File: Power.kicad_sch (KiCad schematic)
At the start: 12 parts, among them J201 Barrel_Jack, U201 AMS1117-3.3, U202 AMS1117-5.0, U203 AMS1117-3.3

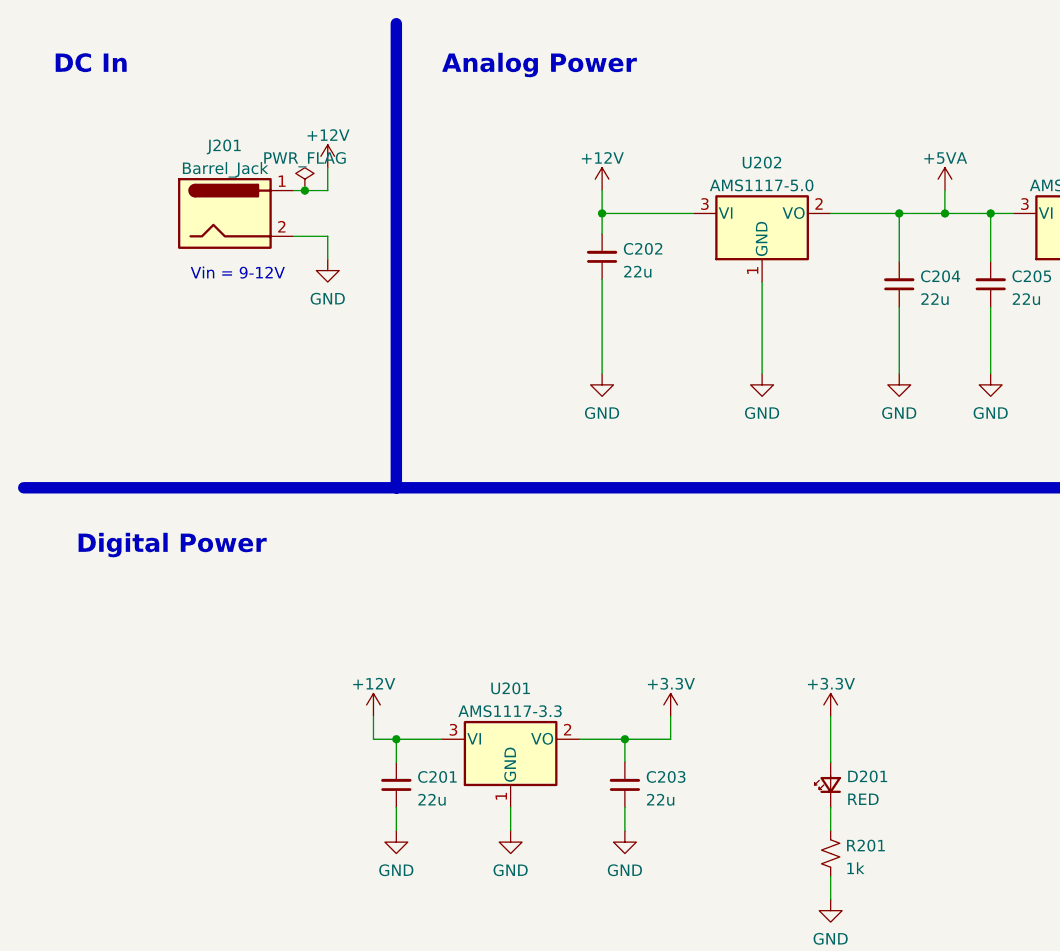
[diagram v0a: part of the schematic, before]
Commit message: Switch ADC
Switched from the ADS1115 to ADS7924 to get faster sampling time.
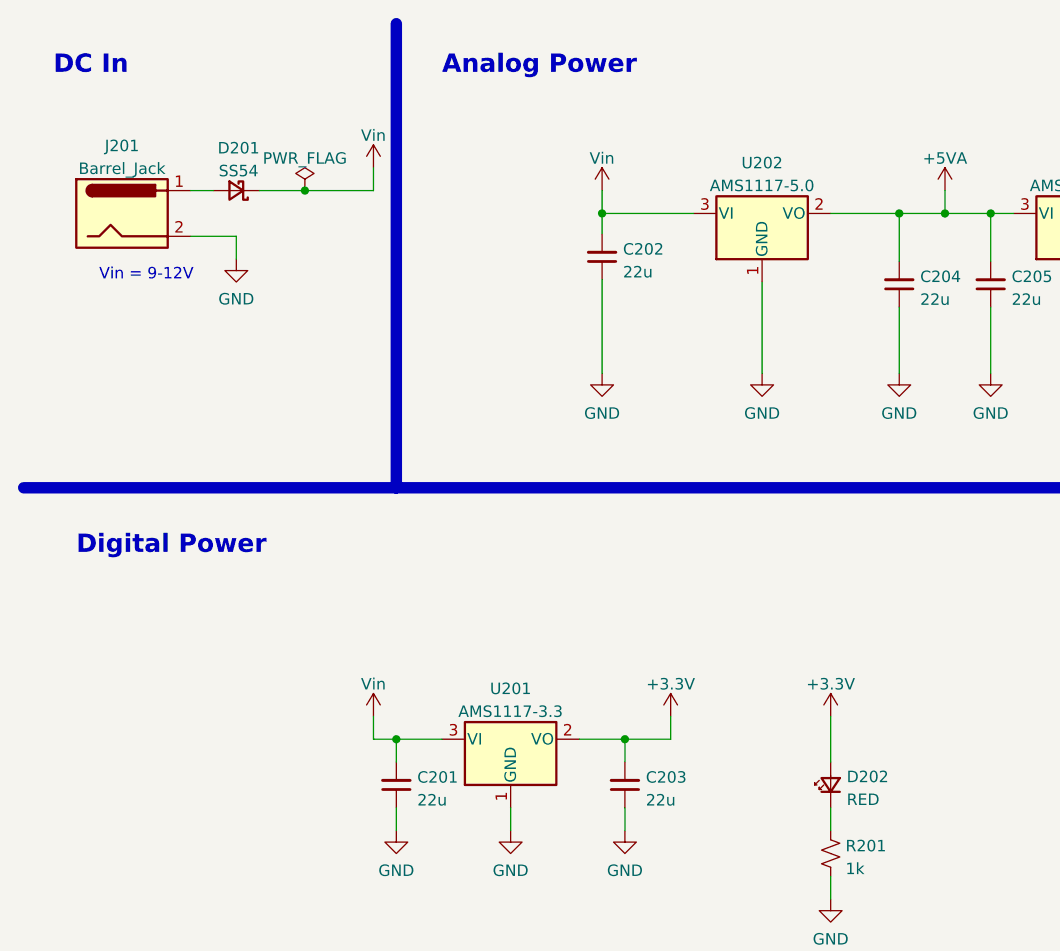
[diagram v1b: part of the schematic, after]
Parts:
- added D201: SS54, Diode_SMD:D_SMA, symbol Device:D_Schottky_Small
- renumbered D201 to D202
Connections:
- net +12V renamed Vin
- net Vin: now also D201.1 (K); no longer J201.1
- new net: D201.2 (A), J201.1
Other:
- moved on the sheet: J201
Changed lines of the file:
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@@
   (junction (at 119.38 33.02) (diameter 0) (color 0 0 0 0)
   )
+  (junction (at 43.18 30.48) (diameter 0) (color 0 0 0 0)
+  )
   (junction (at 109.22 33.02) (diameter 0) (color 0 0 0 0)
   )
@@
   (junction (at 78.74 91.44) (diameter 0) (color 0 0 0 0)
   )
-  (junction (at 43.18 30.48) (diameter 0) (color 0 0 0 0)
-  )
   (wire (pts (xy 101.6 33.02) (xy 109.22 33.02))
     (stroke (width 0) (type default) (color 0 0 0 0))
@@
     (stroke (width 0) (type default) (color 0 0 0 0))
   )
-  (wire (pts (xy 41.91 30.48) (xy 43.18 30.48))
-    (stroke (width 0) (type default) (color 0 0 0 0))
-  )
   (wire (pts (xy 139.7 40.64) (xy 139.7 50.8))
     (stroke (width 0) (type default) (color 0 0 0 0))
@@
     (stroke (width 0) (type default) (color 0 0 0 0))
   )
-  (wire (pts (xy 41.91 35.56) (xy 45.72 35.56))
+  (wire (pts (xy 38.1 30.48) (xy 43.18 30.48))
+    (stroke (width 0) (type default) (color 0 0 0 0))
+  )
+  (wire (pts (xy 30.48 35.56) (xy 35.56 35.56))
     (stroke (width 0) (type default) (color 0 0 0 0))
   )
@@
   )
   (wire (pts (xy 101.6 88.9) (xy 101.6 93.98))
+    (stroke (width 0) (type default) (color 0 0 0 0))
+  )
+  (wire (pts (xy 30.48 30.48) (xy 33.02 30.48))
     (stroke (width 0) (type default) (color 0 0 0 0))
   )
@@
     (stroke (width 0) (type default) (color 0 0 0 0))
   )
-  (wire (pts (xy 45.72 35.56) (xy 45.72 38.1))
+  (wire (pts (xy 35.56 35.56) (xy 35.56 38.1))
     (stroke (width 0) (type default) (color 0 0 0 0))
   )
@@
   )
   (wire (pts (xy 76.2 40.386) (xy 76.2 50.8))
+    (stroke (width 0) (type default) (color 0 0 0 0))
+  )
+  (wire (pts (xy 50.8 27.94) (xy 50.8 30.48))
     (stroke (width 0) (type default) (color 0 0 0 0))
   )
@@
     (stroke (width 0) (type default) (color 0 0 0 0))
   )
-  (wire (pts (xy 45.72 30.48) (xy 45.72 27.94))
-    (stroke (width 0) (type default) (color 0 0 0 0))
-  )
   (wire (pts (xy 139.7 33.02) (xy 139.7 35.56))
     (stroke (width 0) (type default) (color 0 0 0 0))
@@
     (stroke (width 0) (type default) (color 0 0 0 0))
   )
+  (wire (pts (xy 43.18 30.48) (xy 50.8 30.48))
+    (stroke (width 0) (type default) (color 0 0 0 0))
+  )
   (wire (pts (xy 78.74 99.06) (xy 78.74 101.6))
     (stroke (width 0) (type default) (color 0 0 0 0))
   )
   (wire (pts (xy 129.54 40.64) (xy 129.54 50.8))
-    (stroke (width 0) (type default) (color 0 0 0 0))
-  )
-  (wire (pts (xy 43.18 30.48) (xy 45.72 30.48))
     (stroke (width 0) (type default) (color 0 0 0 0))
   )
@@
     (stroke (width 1.27) (type default) (color 0 0 0 0))
   )
-  (text "Vin = 9-12V" (at 30.48 40.64 0)
+  (text "Vin = 9-12V" (at 20.32 40.64 0)
     (effects (font (size 1.27 1.27)) (justify left bottom))
   )
@@
     (pin "1")
     (pin "2")
+  )
+  (symbol (lib_id "power:Vin") (at 50.8 88.9 0) (unit 1)
+    (in_bom yes) (on_board yes) (fields_autoplaced)
+    (property "Reference" "#PWR0104" (id 0) (at 50.8 92.71 0)
+      (effects (font (size 1.27 1.27)) hide)
+    )
+    (property "Value" "Vin" (id 1) (at 50.8 85.3242 0))
+    (property "Footprint" "" (id 2) (at 50.8 88.9 0)
+      (effects (font (size 1.27 1.27)) hide)
+    )
+    (property "Datasheet" "" (id 3) (at 50.8 88.9 0)
+      (effects (font (size 1.27 1.27)) hide)
+    )
+    (pin "1")
+  )
+  (symbol (lib_name "Vin_1") (lib_id "power:Vin") (at 50.8 27.94 0) (unit 1)
+    (in_bom yes) (on_board yes) (fields_autoplaced)
+    (property "Reference" "#PWR0103" (id 0) (at 50.8 31.75 0)
+      (effects (font (size 1.27 1.27)) hide)
+    )
+    (property "Value" "Vin" (id 1) (at 50.8 24.3642 0))
+    (property "Footprint" "" (id 2) (at 50.8 27.94 0)
+      (effects (font (size 1.27 1.27)) hide)
+    )
+    (property "Datasheet" "" (id 3) (at 50.8 27.94 0)
+      (effects (font (size 1.27 1.27)) hide)
+    )
+    (pin "1")
   )
   (symbol (lib_id "power:GND") (at 53.34 101.6 0) (unit 1)
@@
   (symbol (lib_id "Device:LED_Small") (at 101.6 96.52 90) (unit 1)
     (in_bom yes) (on_board yes) (fields_autoplaced)
-    (property "Reference" "D201" (id 0) (at 103.378 95.6218 90)
+    (property "Reference" "D202" (id 0) (at 103.378 95.6218 90)
       (effects (font (size 1.27 1.27)) (justify right))
     )
@@
     (pin "2")
   )
-  (symbol (lib_id "power:+12V") (at 50.8 88.9 0) (unit 1)
-    (in_bom yes) (on_board yes) (fields_autoplaced)
-    (property "Reference" "#PWR0203" (id 0) (at 50.8 92.71 0)
-      (effects (font (size 1.27 1.27)) hide)
-    )
-    (property "Value" "+12V" (id 1) (at 50.8 85.3242 0))
-    (property "Footprint" "" (id 2) (at 50.8 88.9 0)
-      (effects (font (size 1.27 1.27)) hide)
-    )
-    (property "Datasheet" "" (id 3) (at 50.8 88.9 0)
+  (symbol (lib_name "Vin_2") (lib_id "power:Vin") (at 76.2 30.48 0) (unit 1)
+    (in_bom yes) (on_board yes) (fields_autoplaced)
+    (property "Reference" "#PWR0102" (id 0) (at 76.2 34.29 0)
+      (effects (font (size 1.27 1.27)) hide)
+    )
+    (property "Value" "Vin" (id 1) (at 76.2 26.9042 0))
+    (property "Footprint" "" (id 2) (at 76.2 30.48 0)
+      (effects (font (size 1.27 1.27)) hide)
+    )
+    (property "Datasheet" "" (id 3) (at 76.2 30.48 0)
       (effects (font (size 1.27 1.27)) hide)
     )
@@
     (pin "1")
   )
-  (symbol (lib_id "Connector:Barrel_Jack") (at 34.29 33.02 0) (unit 1)
-    (in_bom yes) (on_board yes) (fields_autoplaced)
-    (property "Reference" "J201" (id 0) (at 34.29 25.5102 0))
-    (property "Value" "Barrel_Jack" (id 1) (at 34.29 28.0471 0))
-    (property "Footprint" "Connector_BarrelJack:BarrelJack_Horizontal" (id 2) (at 35.56 34.036 0)
-      (effects (font (size 1.27 1.27)) hide)
-    )
-    (property "Datasheet" "~" (id 3) (at 35.56 34.036 0)
+  (symbol (lib_id "Connector:Barrel_Jack") (at 22.86 33.02 0) (unit 1)
+    (in_bom yes) (on_board yes) (fields_autoplaced)
+    (property "Reference" "J201" (id 0) (at 22.86 25.5102 0))
+    (property "Value" "Barrel_Jack" (id 1) (at 22.86 28.0471 0))
+    (property "Footprint" "Connector_BarrelJack:BarrelJack_Horizontal" (id 2) (at 24.13 34.036 0)
+      (effects (font (size 1.27 1.27)) hide)
+    )
+    (property "Datasheet" "~" (id 3) (at 24.13 34.036 0)
       (effects (font (size 1.27 1.27)) hide)
     )
@@
     (pin "1")
   )
-  (symbol (lib_id "power:+12V") (at 45.72 27.94 0) (unit 1)
-    (in_bom yes) (on_board yes) (fields_autoplaced)
-    (property "Reference" "#PWR0201" (id 0) (at 45.72 31.75 0)
-      (effects (font (size 1.27 1.27)) hide)
-    )
-    (property "Value" "+12V" (id 1) (at 45.72 24.3642 0))
-    (property "Footprint" "" (id 2) (at 45.72 27.94 0)
-      (effects (font (size 1.27 1.27)) hide)
-    )
-    (property "Datasheet" "" (id 3) (at 45.72 27.94 0)
-      (effects (font (size 1.27 1.27)) hide)
-    )
-    (pin "1")
-  )
   (symbol (lib_id "power:+3.3V") (at 101.6 88.9 0) (unit 1)
     (in_bom yes) (on_board yes) (fields_autoplaced)
@@
     (pin "1")
   )
-  (symbol (lib_id "power:GND") (at 45.72 38.1 0) (unit 1)
-    (in_bom yes) (on_board yes) (fields_autoplaced)
-    (property "Reference" "#PWR0202" (id 0) (at 45.72 44.45 0)
-      (effects (font (size 1.27 1.27)) hide)
-    )
-    (property "Value" "GND" (id 1) (at 45.72 42.5434 0))
-    (property "Footprint" "" (id 2) (at 45.72 38.1 0)
-      (effects (font (size 1.27 1.27)) hide)
-    )
-    (property "Datasheet" "" (id 3) (at 45.72 38.1 0)
-      (effects (font (size 1.27 1.27)) hide)
-    )
-    (pin "1")
+  (symbol (lib_id "power:GND") (at 35.56 38.1 0) (unit 1)
+    (in_bom yes) (on_board yes) (fields_autoplaced)
+    (property "Reference" "#PWR0201" (id 0) (at 35.56 44.45 0)
+      (effects (font (size 1.27 1.27)) hide)
+    )
+    (property "Value" "GND" (id 1) (at 35.56 42.5434 0))
+    (property "Footprint" "" (id 2) (at 35.56 38.1 0)
+      (effects (font (size 1.27 1.27)) hide)
+    )
+    (property "Datasheet" "" (id 3) (at 35.56 38.1 0)
+      (effects (font (size 1.27 1.27)) hide)
+    )
+    (pin "1")
+  )
+  (symbol (lib_id "Device:D_Schottky_Small") (at 35.56 30.48 180) (unit 1)
+    (in_bom yes) (on_board yes) (fields_autoplaced)
+    (property "Reference" "D201" (id 0) (at 35.814 25.7642 0))
+    (property "Value" "SS54" (id 1) (at 35.814 28.3011 0))
+    (property "Footprint" "Diode_SMD:D_SMA" (id 2) (at 35.56 30.48 90)
+      (effects (font (size 1.27 1.27)) hide)
+    )
+    (property "Datasheet" "~" (id 3) (at 35.56 30.48 90)
+      (effects (font (size 1.27 1.27)) hide)
+    )
+    (property "LCSC" "C22452" (id 4) (at 35.56 30.48 0)
+      (effects (font (size 1.27 1.27)) hide)
+    )
+    (pin "1")
+    (pin "2")
   )
   (symbol (lib_id "Regulator_Linear:AMS1117-3.3") (at 66.04 91.44 0) (unit 1)
@@
       (effects (font (size 1.27 1.27)) hide)
     )
-    (pin "1")
-  )
-  (symbol (lib_id "power:+12V") (at 76.2 30.48 0) (unit 1)
-    (in_bom yes) (on_board yes) (fields_autoplaced)
-    (property "Reference" "#PWR0206" (id 0) (at 76.2 34.29 0)
-      (effects (font (size 1.27 1.27)) hide)
-    )
-    (property "Value" "+12V" (id 1) (at 76.2 26.9042 0))
-    (property "Footprint" "" (id 2) (at 76.2 30.48 0)
-      (effects (font (size 1.27 1.27)) hide)
-    )
-    (property "Datasheet" "" (id 3) (at 76.2 30.48 0)
-      (effects (font (size 1.27 1.27)) hide)
-    )

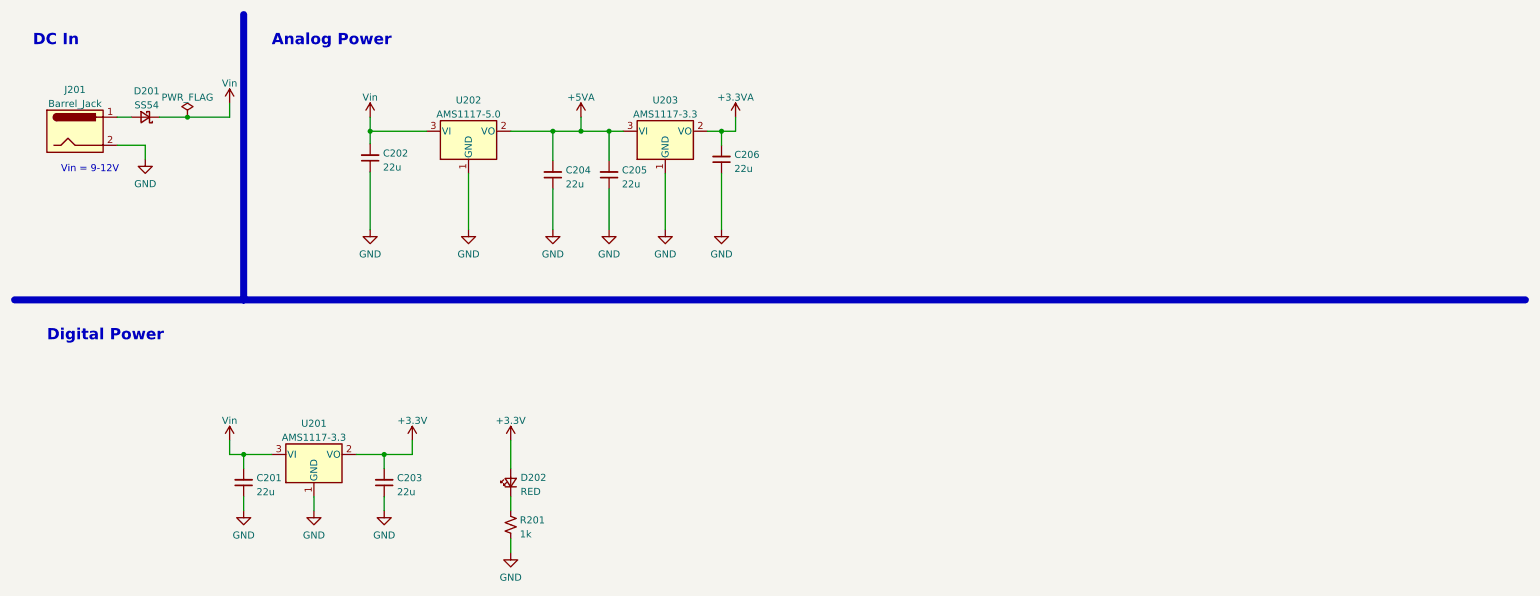
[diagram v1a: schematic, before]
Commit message: Improvements
Switched ADC to ADC128S.
Upgraded USB to USB-C
Improved Analog front end to work with signals better.
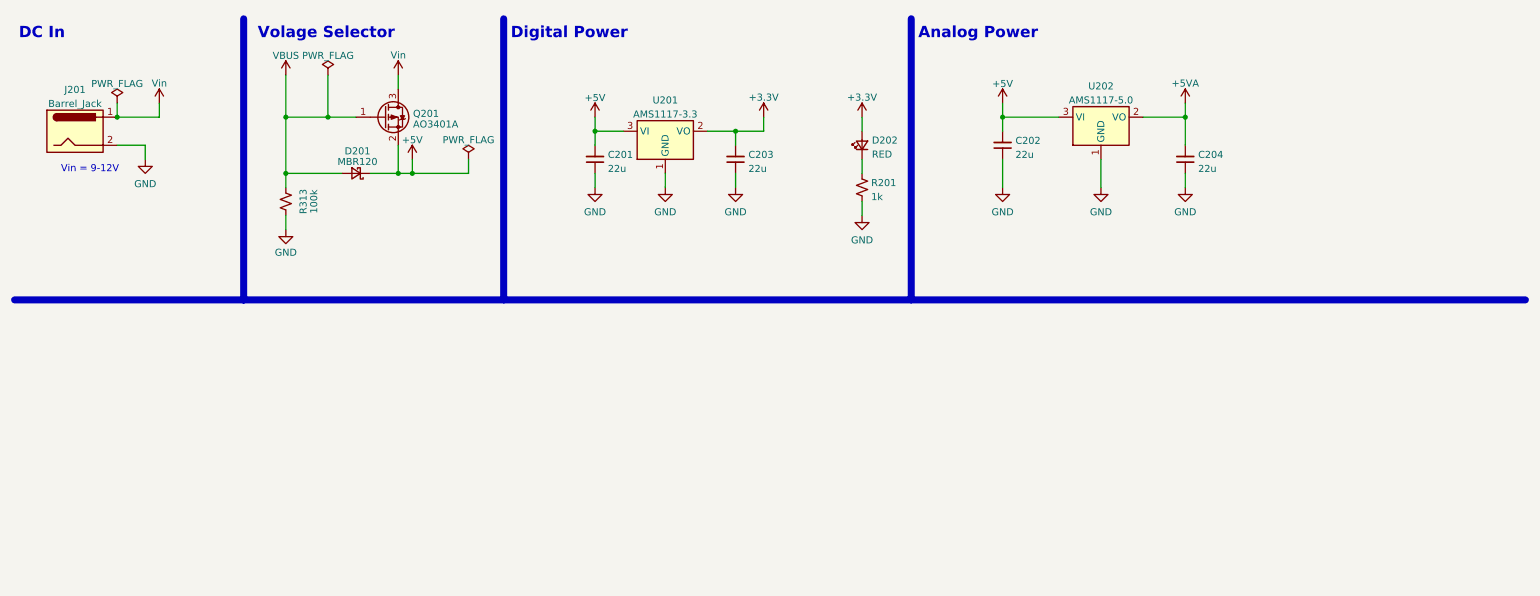
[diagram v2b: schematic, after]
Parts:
- removed C205, C206: 22u, Capacitor_SMD:C_0805_2012Metric, symbol Device:C_Small
- removed U203: AMS1117-3.3, Package_TO_SOT_SMD:SOT-223-3_TabPin2, symbol Regulator_Linear:AMS1117-3.3
- added Q201: AO3401A, Package_TO_SOT_SMD:SOT-23, symbol Transistor_FET:AO3401A
- added R313: 100k, Resistor_SMD:R_0402_1005Metric, symbol Device:R_Small_US
- D201: value SS54 -> MBR120; footprint Diode_SMD:D_SMA -> Diode_SMD:D_SOD-123; LCSC C22452 -> C130880
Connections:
- net GND: now also R313.1
- net Vin: now also J201.1, Q201.3 (D); no longer C201.2, C202.2, D201.1 (K), U201.3 (VI), U202.3 (VI)
- net VBUS: now reaches D201.2 (A)
- net VBUS: now also Q201.1 (G), R313.2; no longer J201.1
- new net +5V: C201.2, C202.2, D201.1 (K), Q201.2 (S), U201.3 (VI), U202.3 (VI)
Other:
- note added: "Volage Selector"
